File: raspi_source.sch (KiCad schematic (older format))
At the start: 18 parts, among them J1 Conn_01x02_Female, J2 Conn_01x01_Female, J3 Conn_01x01_Female, J4 Conn_01x01_Female, J5 Conn_01x02_Female, Q1 2N7000, Q2 DMG3415U, U1 OKL-T

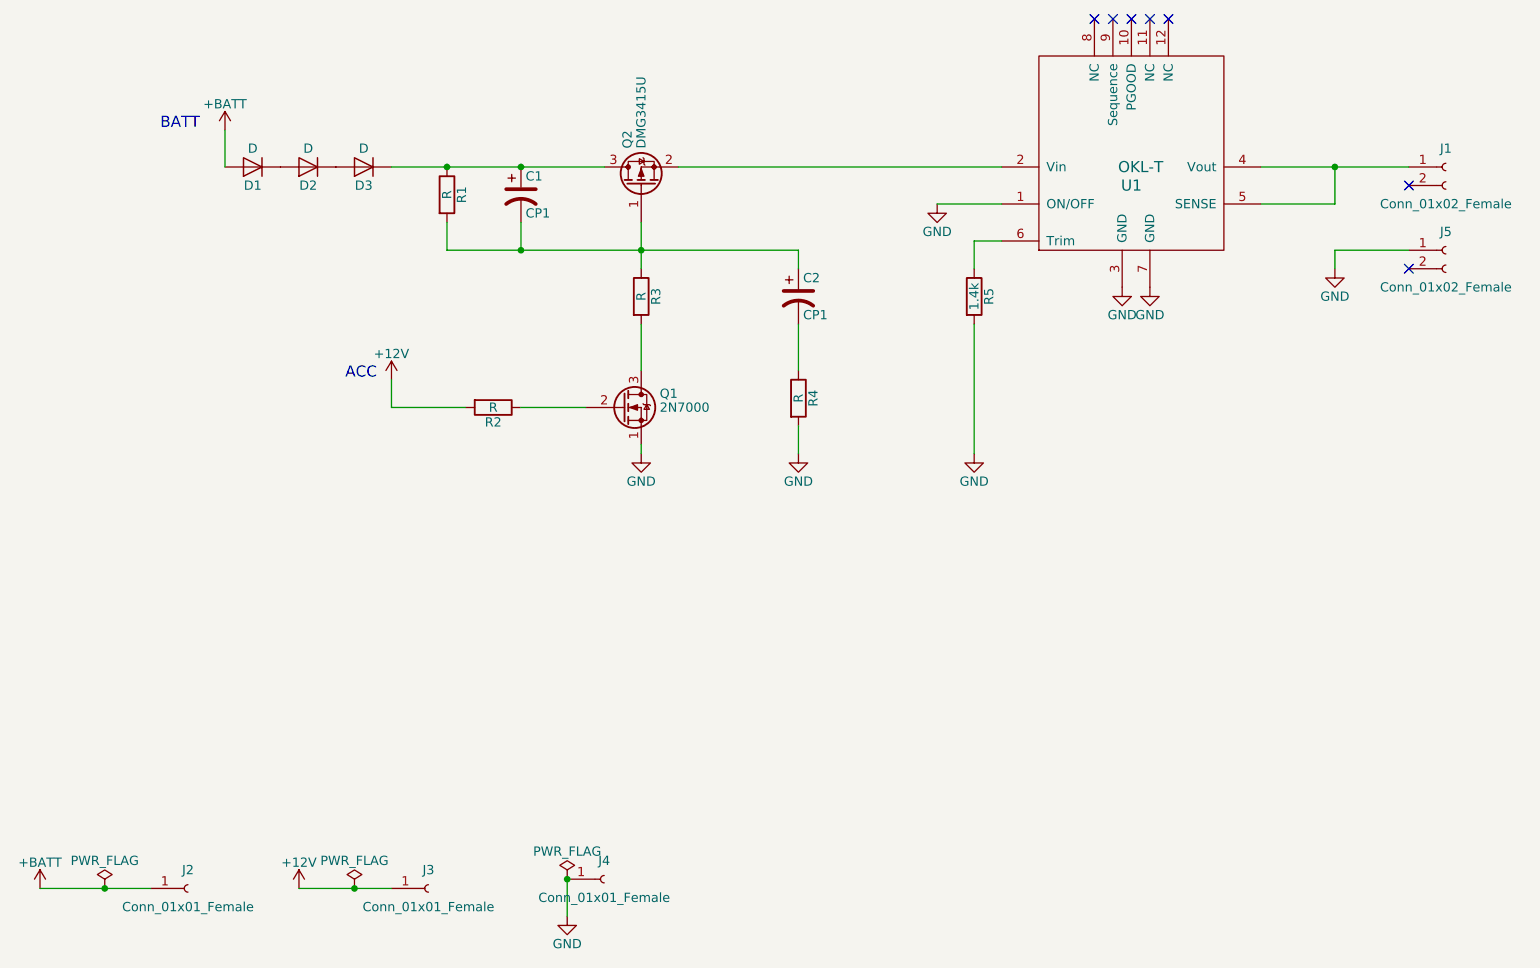
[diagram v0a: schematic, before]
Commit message: the scheme has been complete.
test has been passed and the scheme was modified
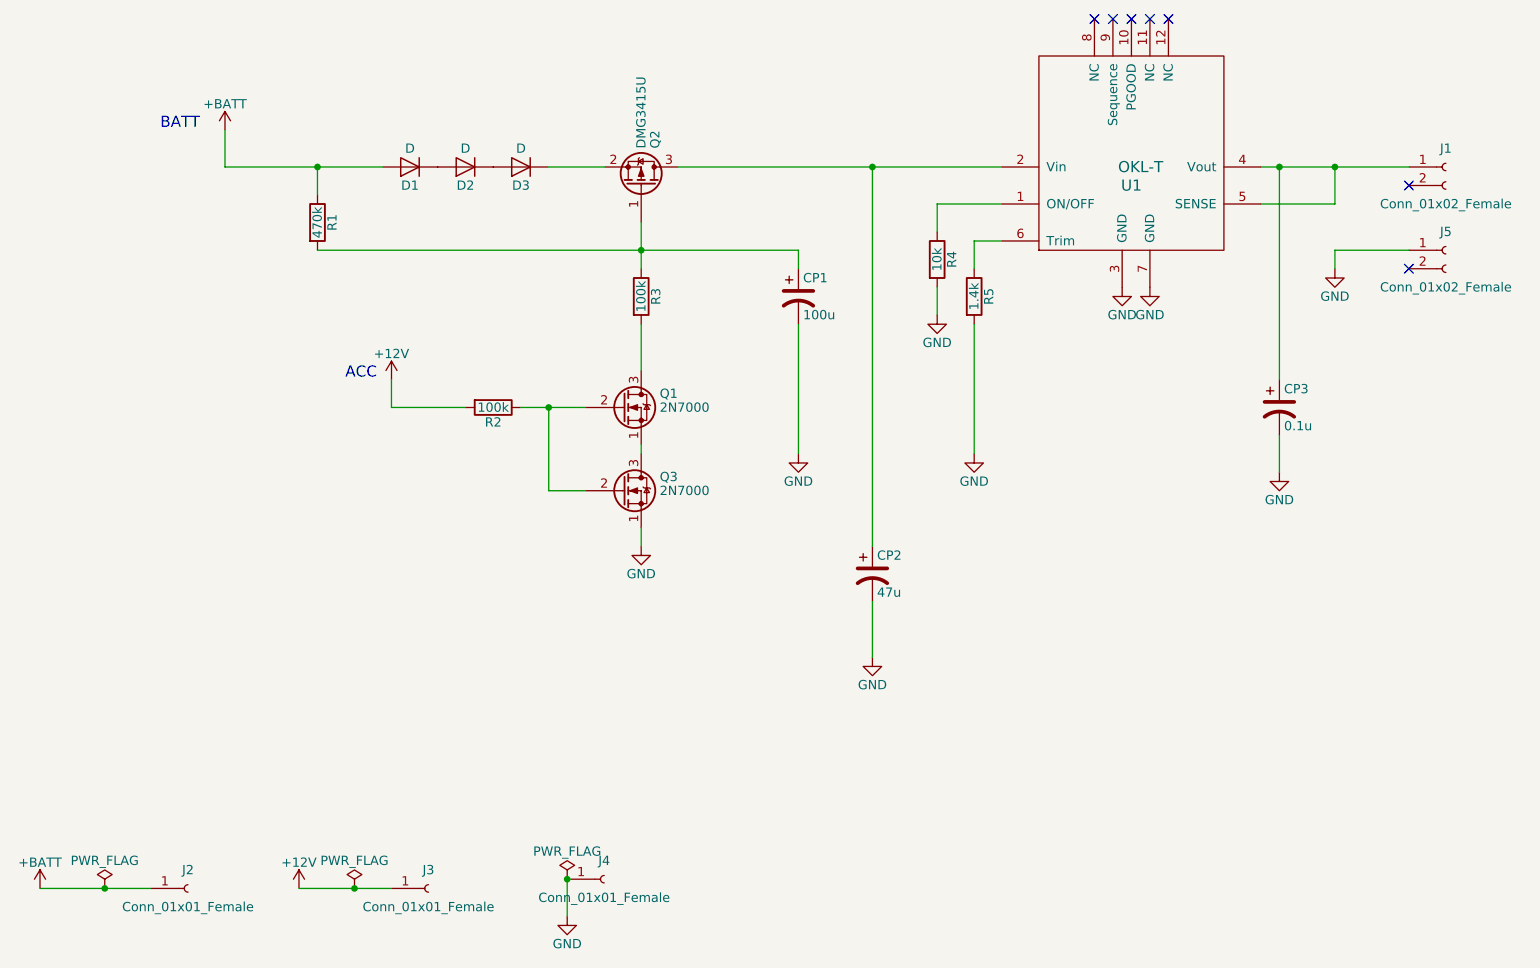
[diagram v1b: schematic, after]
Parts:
- removed C1: CP1, Capacitors_THT:CP_Radial_Tantal_D4.5mm_P2.50mm, symbol CP1
- added CP2: 47u, Capacitors_THT:CP_Radial_Tantal_D4.5mm_P2.50mm, symbol CP1
- added CP3: 0.1u, Capacitors_THT:CP_Radial_Tantal_D4.5mm_P2.50mm, symbol CP1
- added Q3: 2N7000, TO_SOT_Packages_THT:TO-92_Molded_Narrow, symbol 2N7000
- CP1: renamed from C2; value CP1 -> 100u
- R1: value R -> 470k
- R2, R3: value R -> 100k
- R4: value R -> 10k
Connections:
- net +BATT: now also R1.1
- net GND: now also CP1.2, CP2.2, CP3.2, Q3.1 (S); no longer Q1.1 (S), U1.1 (ON/OFF)
- net at Q1.2 (G), R2.1: now also Q3.2 (G)
- net at R4.1: now also U1.1 (ON/OFF); no longer CP1.2
- net at U1.2 (Vin): now also Q2.3 (D), CP2.1; no longer Q2.2 (S)
- net at J1.1 (Pin_1), U1.4 (Vout), U1.5 (SENSE): now also CP3.1
- new net: Q1.1 (S), Q3.3 (D)
- new net: D3.1 (K), Q2.2 (S)
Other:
- moved on the sheet: D1, D2, D3, R1

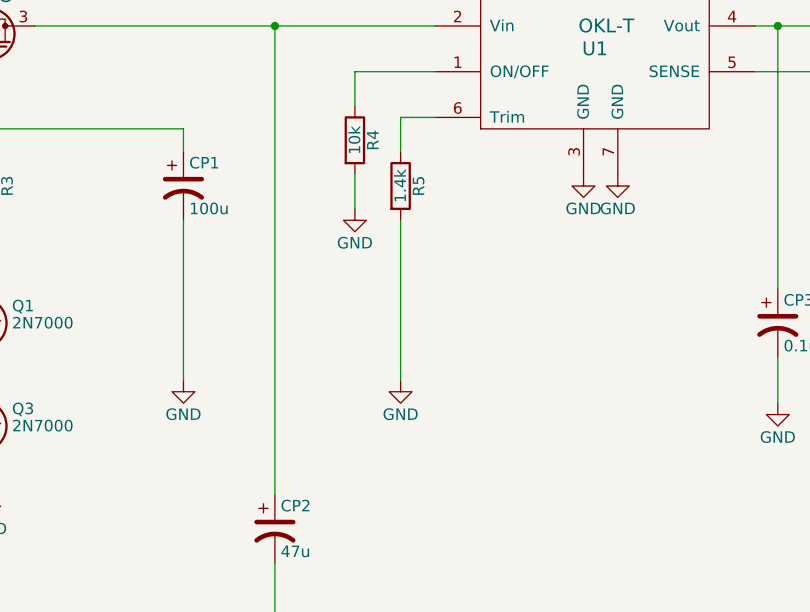
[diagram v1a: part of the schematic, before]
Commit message: adjust dcdc register
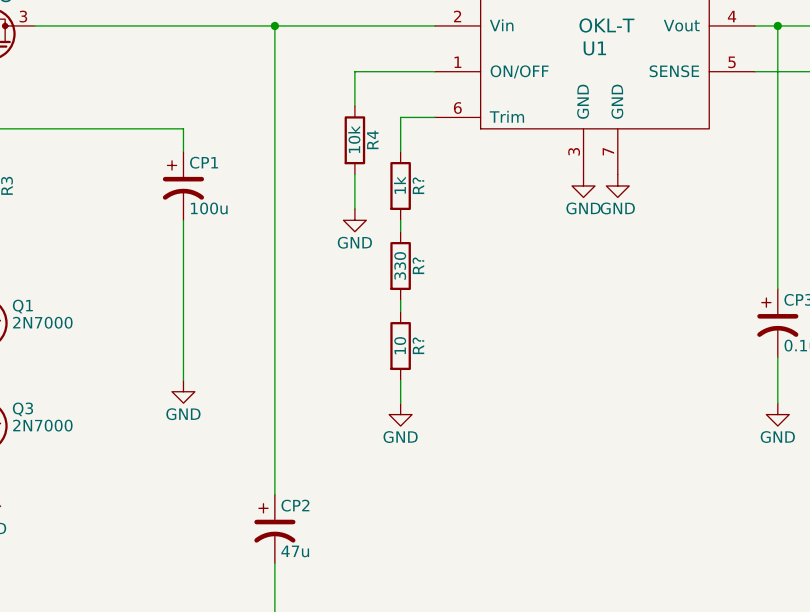
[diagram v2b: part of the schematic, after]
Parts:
- removed R5: 1.4k, Resistors_THT:R_Axial_DIN0204_L3.6mm_D1.6mm_P7.62mm_Horizontal, symbol R
- added R?: 1k, symbol R
- added R?: 330, symbol R
- added R?: 10, symbol R
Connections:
- net GND: now also R?.2
- net at U1.6 (Trim): now also R?.1
- new net: R?.1, R?.2 (x2)
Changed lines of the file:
@@
-$EndComp
-$Comp
-L R R5
-U 1 1 5B139294
-P 6050 2750
-F 0 "R5" V 6130 2750 50  0000 C CNN
-F 1 "1.4k" V 6050 2750 50  0000 C CNN
-F 2 "Resistors_THT:R_Axial_DIN0204_L3.6mm_D1.6mm_P7.62mm_Horizontal" V 5980 2750 50  0001 C CNN
-F 3 "" H 6050 2750 50  0001 C CNN
-	1    6050 2750
-	1    0    0    -1
 $EndComp
 $Comp
@@
 L GND #PWR10
 U 1 1 5B13AACA
-P 6050 3600
-F 0 "#PWR10" H 6050 3350 50  0001 C CNN
-F 1 "GND" H 6050 3450 50  0000 C CNN
-F 2 "" H 6050 3600 50  0001 C CNN
-F 3 "" H 6050 3600 50  0001 C CNN
-	1    6050 3600
+P 6050 3700
+F 0 "#PWR10" H 6050 3450 50  0001 C CNN
+F 1 "GND" H 6050 3550 50  0000 C CNN
+F 2 "" H 6050 3700 50  0001 C CNN
+F 3 "" H 6050 3700 50  0001 C CNN
+	1    6050 3700
 	1    0    0    -1
 $EndComp
@@
 	5100 2900 5100 3600
 Wire Wire Line
-	6050 2900 6050 3600
-Wire Wire Line
 	6200 2250 5850 2250
 Wire Wire Line
@@
 Wire Wire Line
 	3750 2050 4050 2050
+$Comp
+L R R?
+U 1 1 5B1C8D3A
+P 6050 2750
+F 0 "R?" V 6130 2750 50  0000 C CNN
+F 1 "1k" V 6050 2750 50  0000 C CNN
+F 2 "" V 5980 2750 50  0001 C CNN
+F 3 "" H 6050 2750 50  0001 C CNN
+	1    6050 2750
+	1    0    0    -1
+$EndComp
+$Comp
+L R R?
+U 1 1 5B1C8DB3
+P 6050 3100
+F 0 "R?" V 6130 3100 50  0000 C CNN
+F 1 "330" V 6050 3100 50  0000 C CNN
+F 2 "" V 5980 3100 50  0001 C CNN
+F 3 "" H 6050 3100 50  0001 C CNN
+	1    6050 3100
+	1    0    0    -1
+$EndComp
+$Comp
+L R R?
+U 1 1 5B1C8E29
+P 6050 3450
+F 0 "R?" V 6130 3450 50  0000 C CNN
+F 1 "10" V 6050 3450 50  0000 C CNN
+F 2 "" V 5980 3450 50  0001 C CNN
+F 3 "" H 6050 3450 50  0001 C CNN
+	1    6050 3450
+	1    0    0    -1
+$EndComp
+Wire Wire Line
+	6050 2900 6050 2950
+Wire Wire Line
+	6050 3250 6050 3300
+Wire Wire Line
+	6050 3600 6050 3700
 $EndSCHEMATC
